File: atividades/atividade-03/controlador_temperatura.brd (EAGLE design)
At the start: 68.6 x 53.3 mm, 34 parts, among them Q1 BC337, Q2 BC337, Q3 BC337

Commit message: heater realinhado
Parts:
- moved R1 33.8 mm to (-118.1, 111.8), turned to 270 degrees
- moved R2 23.3 mm to (-125.7, 123.2), flipped to the bottom, turned to 270 degrees
- moved HTR_LED 22.9 mm to (-83.8, 138.4), turned to 270 degrees
- moved R3 15.3 mm to (-94.0, 133.3), turned to 270 degrees
- moved D1 11.7 mm to (-104.1, 123.2), turned to 90 degrees
- moved HTR 7.18 mm to (-83.8, 120.7), turned to 90 degrees
- moved Q1 1.80 mm to (-115.6, 121.9), flipped to the bottom, turned to 270 degrees

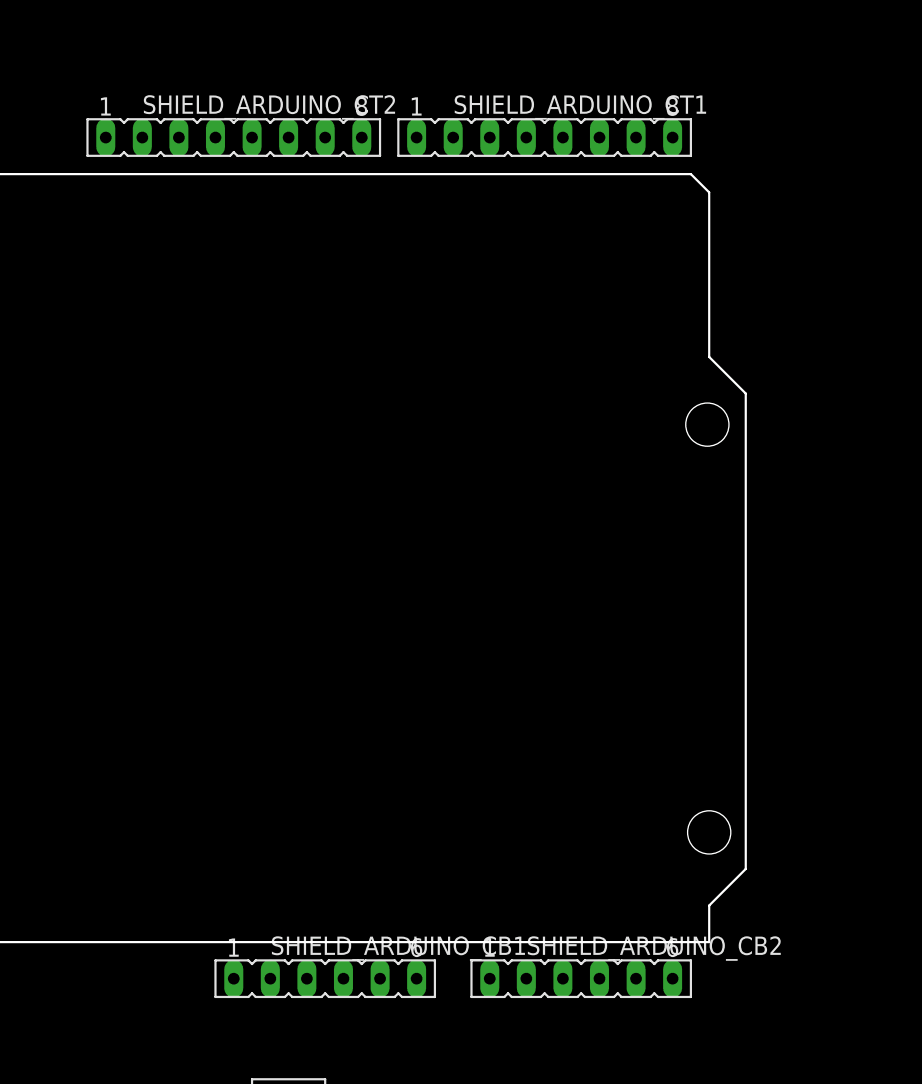
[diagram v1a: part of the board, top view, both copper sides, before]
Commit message: conectores de shield dentro da placa novamente
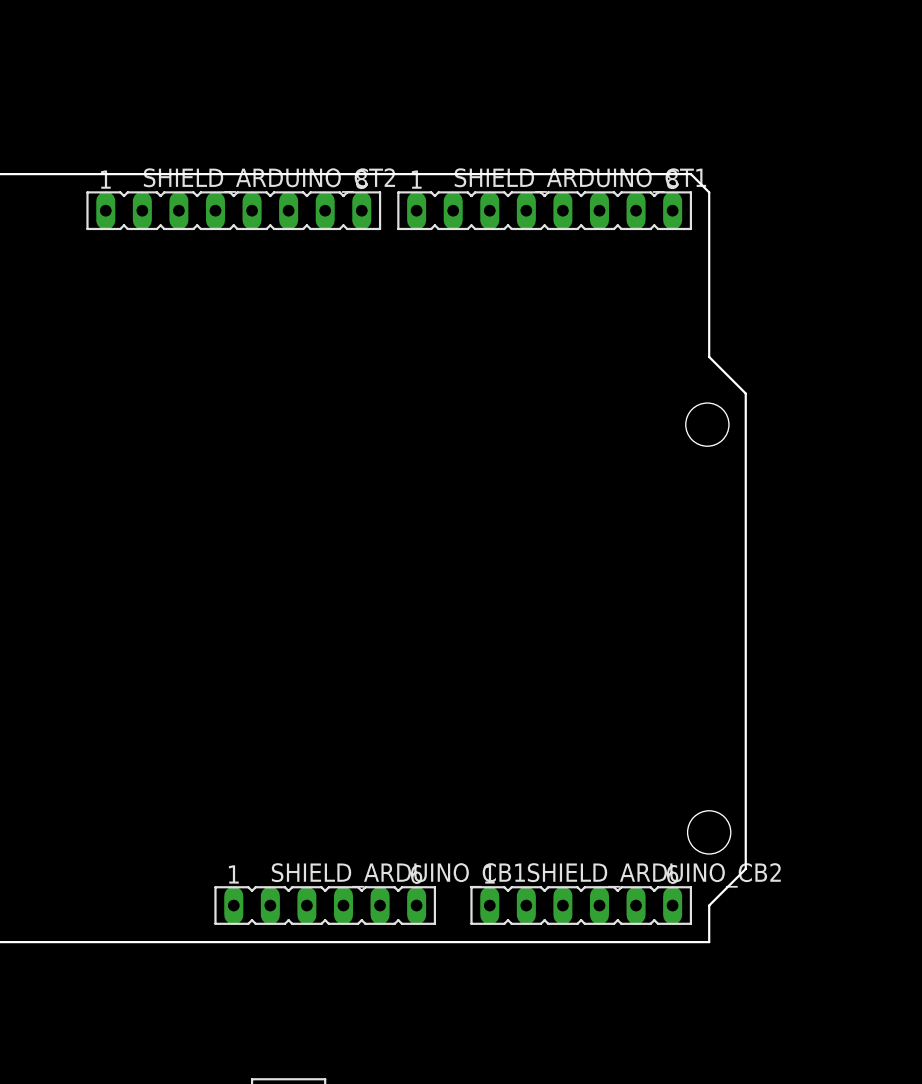
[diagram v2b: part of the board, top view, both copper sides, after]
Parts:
- moved SHIELD_ARDUINO_CT1 5.08 mm to (54.6, 50.8)
- moved SHIELD_ARDUINO_CT2 5.08 mm to (33.0, 50.8)
- moved SHIELD_ARDUINO_CB1 5.08 mm to (39.4, 2.54)
- moved SHIELD_ARDUINO_CB2 5.08 mm to (57.1, 2.54)

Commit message: check point
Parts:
- moved R10 194.5 mm to (57.1, 15.2)
- moved R11 194.5 mm to (59.7, 15.2)
- moved R8 194.5 mm to (52.1, 15.2)
- moved R9 194.5 mm to (54.6, 15.2)
- moved BUTTONS 186.9 mm to (55.9, 7.62)
- moved R12 94.9 mm to (14.0, 27.9), turned to 90 degrees
- moved DS18B20 89.7 mm to (15.2, 40.6), turned to 180 degrees
- moved SHIELD 53.8 mm to (50.8, 43.2)
- moved V1 50.1 mm to (61.0, 29.2)
- moved R6 48.3 mm to (48.3, 31.8)
- moved RST 17.7 mm to (20.3, -5.08)
- moved BUZZ 14.9 mm to (-3.81, -36.8), turned to 0 degrees
- moved R7 7.73 mm to (-3.81, -17.8)
- moved Q3 5.24 mm to (-3.81, -27.9), turned to 0 degrees
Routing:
- net VCC: track 0.00 -> 66.2 mm
- net D7: track 0.00 -> 10.7 mm
- net GND: track 0.00 -> 10.2 mm
- net A0: track 0.00 -> 9.42 mm
- net A3: track 0.00 -> 9.42 mm
- net A2: track 0.00 -> 9.42 mm
- net A1: track 0.00 -> 9.42 mm

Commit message: checkpoint
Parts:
- moved Q3 49.5 mm to (20.3, 15.2)
- moved R7 49.5 mm to (20.3, 25.4)
- moved BUZZ 41.0 mm to (7.62, 2.54)
- moved V1 35.8 mm to (25.4, 33.0)
- moved R6 35.1 mm to (14.0, 39.4), turned to 180 degrees
- moved DS18B20 32.2 mm to (-16.5, 45.7)
- moved R12 29.0 mm to (-12.7, 39.4), turned to 180 degrees
- moved SHIELD 22.2 mm to (59.7, 22.9), flipped to the bottom, turned to 90 degrees
- moved RST 21.6 mm to (35.6, 10.2)
- moved R8 13.3 mm to (39.4, 19.1)
- moved R9 12.0 mm to (43.2, 19.1), flipped to the top
- moved R10 10.9 mm to (47.0, 19.1)
- moved R11 9.67 mm to (50.8, 19.1)
- moved BUTTONS 9.25 mm to (47.0, 10.2)
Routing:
- net A5: track 0.00 -> 20.4 mm
- net A4: track 0.00 -> 16.8 mm
- net VCC: track 66.2 -> 52.1 mm
- net VIN: track 0.00 -> 10.5 mm
- net GND: track 10.2 -> 20.6 mm
- net A2: track 9.42 -> 18.6 mm
- net A0: track 9.42 -> 18.3 mm
- net A3: track 9.42 -> 18.1 mm
- net A1: track 9.42 -> 18.0 mm
- net RST: track 0.00 -> 8.15 mm
- net D7: track 10.7 -> 7.04 mm
